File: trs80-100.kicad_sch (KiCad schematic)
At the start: 181 parts, among them CN2 A-7224, CN3 TCS-4480, CN4 TCS-4490, CN6 RS232C, J1 Adapter Jack CN9, M27 4011, M28 4013, M30 TL064, M33 40H157, M34 4584, M35 4584, SW3 SLB-22BP-03, SW4 Reset Switch, SW5 SSP32201, T10 2SC2603, T11 2SC2603, T13 2SC2603, T14 2SC2603(E), T15 2SC2603(E), T16 2SC2603(E), T17 2SC2603(E), T18 2SC2603, T19 2SA1115, T20 2SC2603, T21 2SC2603(E), T22 2SC2603(E), T25 2SC2603, T27 2SC2603, T28 2SA1115, T6 2SC2603, T9 2SC2603

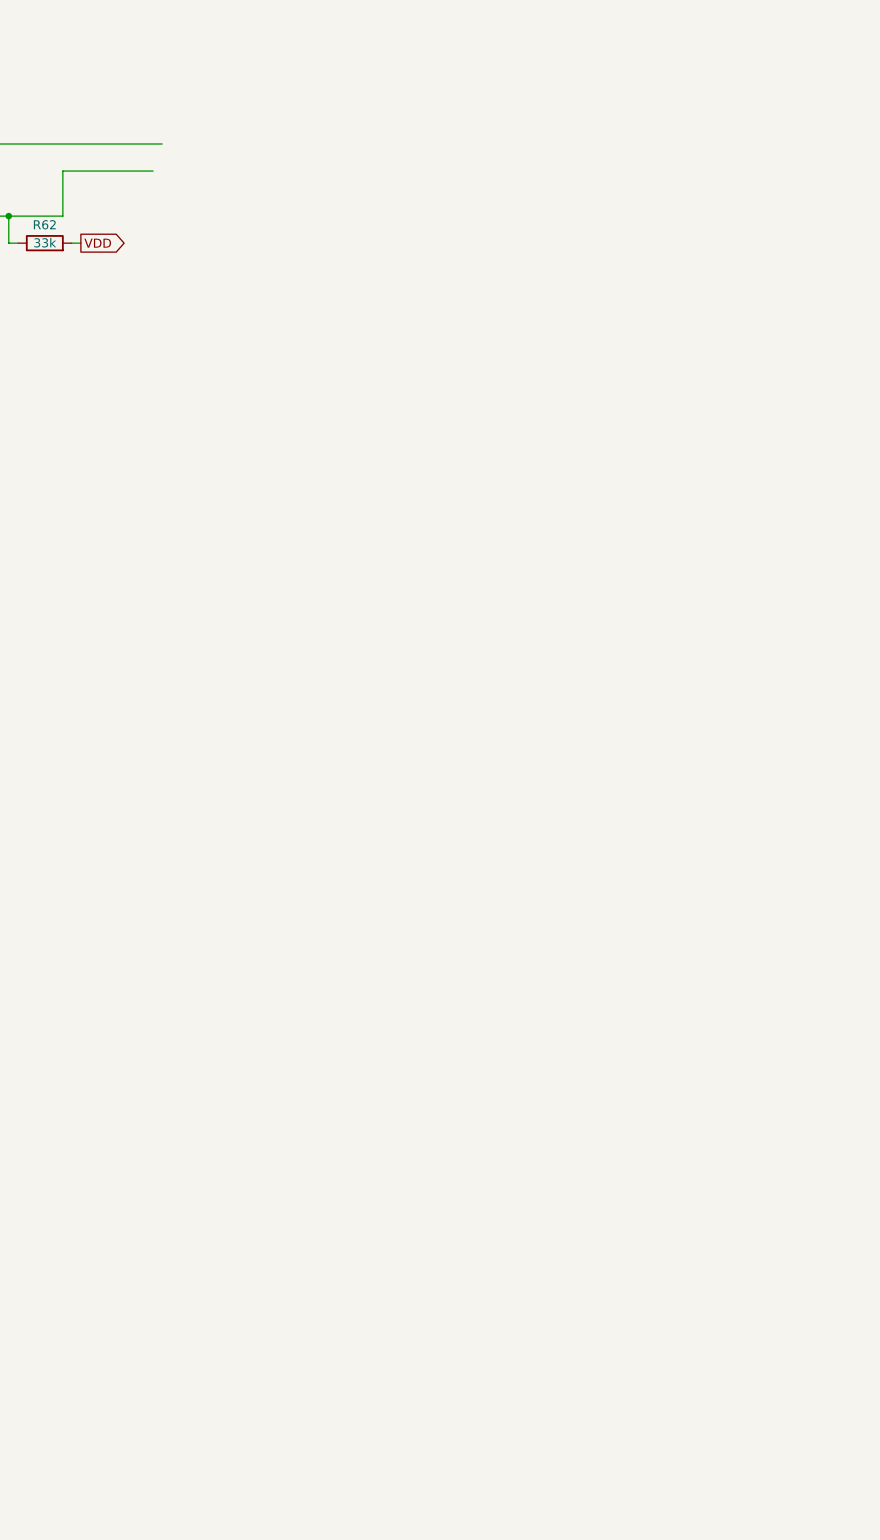
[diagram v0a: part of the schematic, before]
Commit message: Add two different drawings of 40H244 symbol.
Since the schematic is hand-drawn, the pin-out is adapted locally
for the purpose.
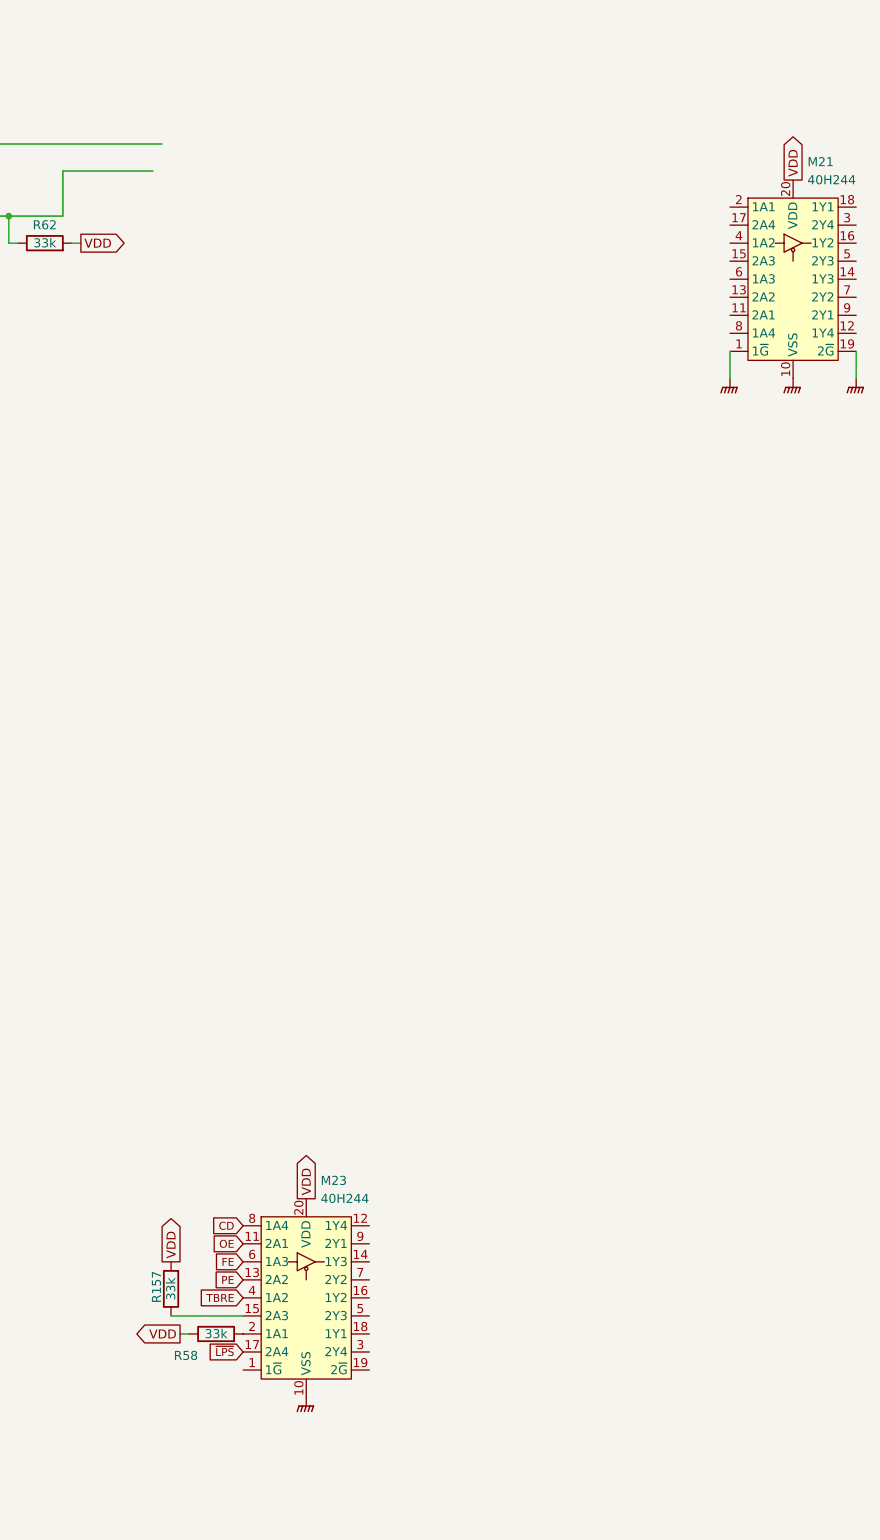
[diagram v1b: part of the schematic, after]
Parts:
- added M21: 40H244, symbol trs80-100:40H244(21)
- added M23: 40H244, symbol trs80-100:40H244(23)
- added R157, R58: 33k, symbol Device:R
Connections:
- net CD: now also M23.8 (1A4)
- net GNDPWR: now also M21.1 (1~{G}), M21.10 (VSS), M21.19 (2~{G}), M23.10 (VSS)
- net VDD: now also M21.20 (VDD), M23.20 (VDD), R157.2, R58.1
- net ~{LPS}: now also M23.17 (2A4)
- new net: M23.2 (1A1), R58.2
- new net: M23.15 (2A3), R157.1
- new net FE: M23.6 (1A3)
- new net OE: M23.11 (2A1)
- new net PE: M23.13 (2A2)
- new net TBRE: M23.4 (1A2)

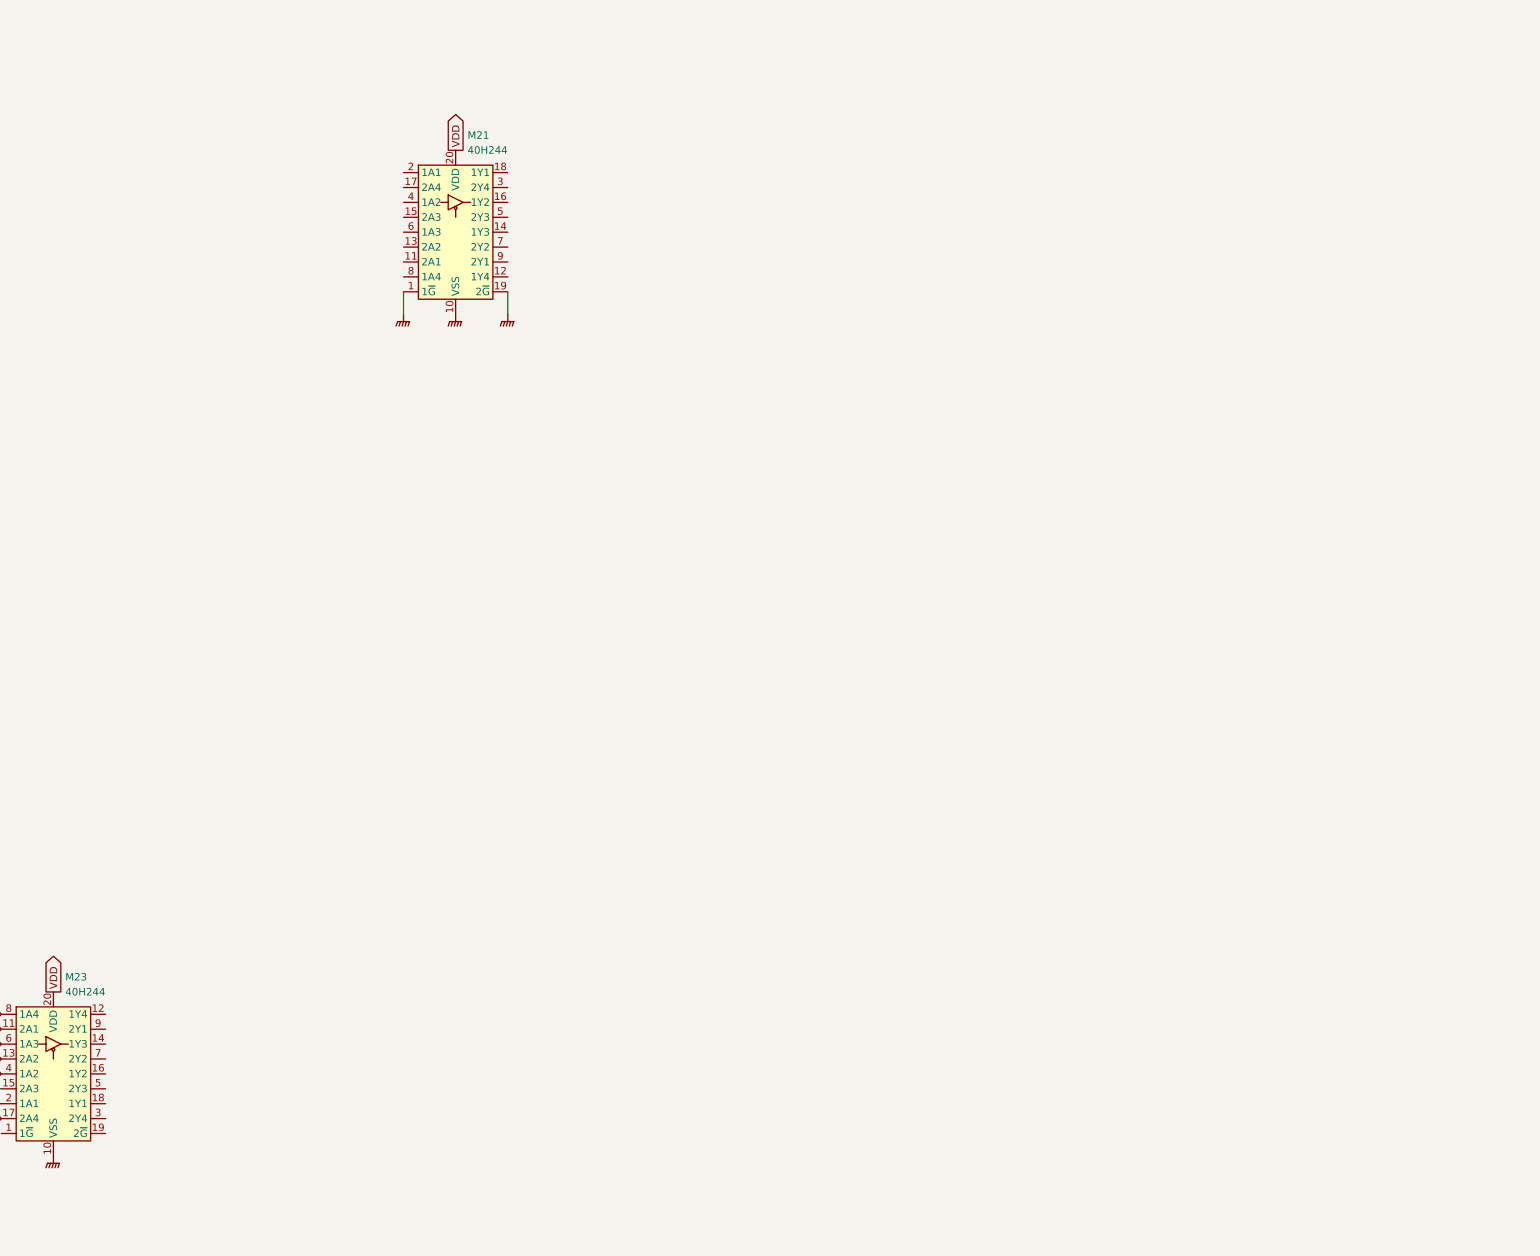
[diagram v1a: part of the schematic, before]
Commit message: Make a keyboard symbol.
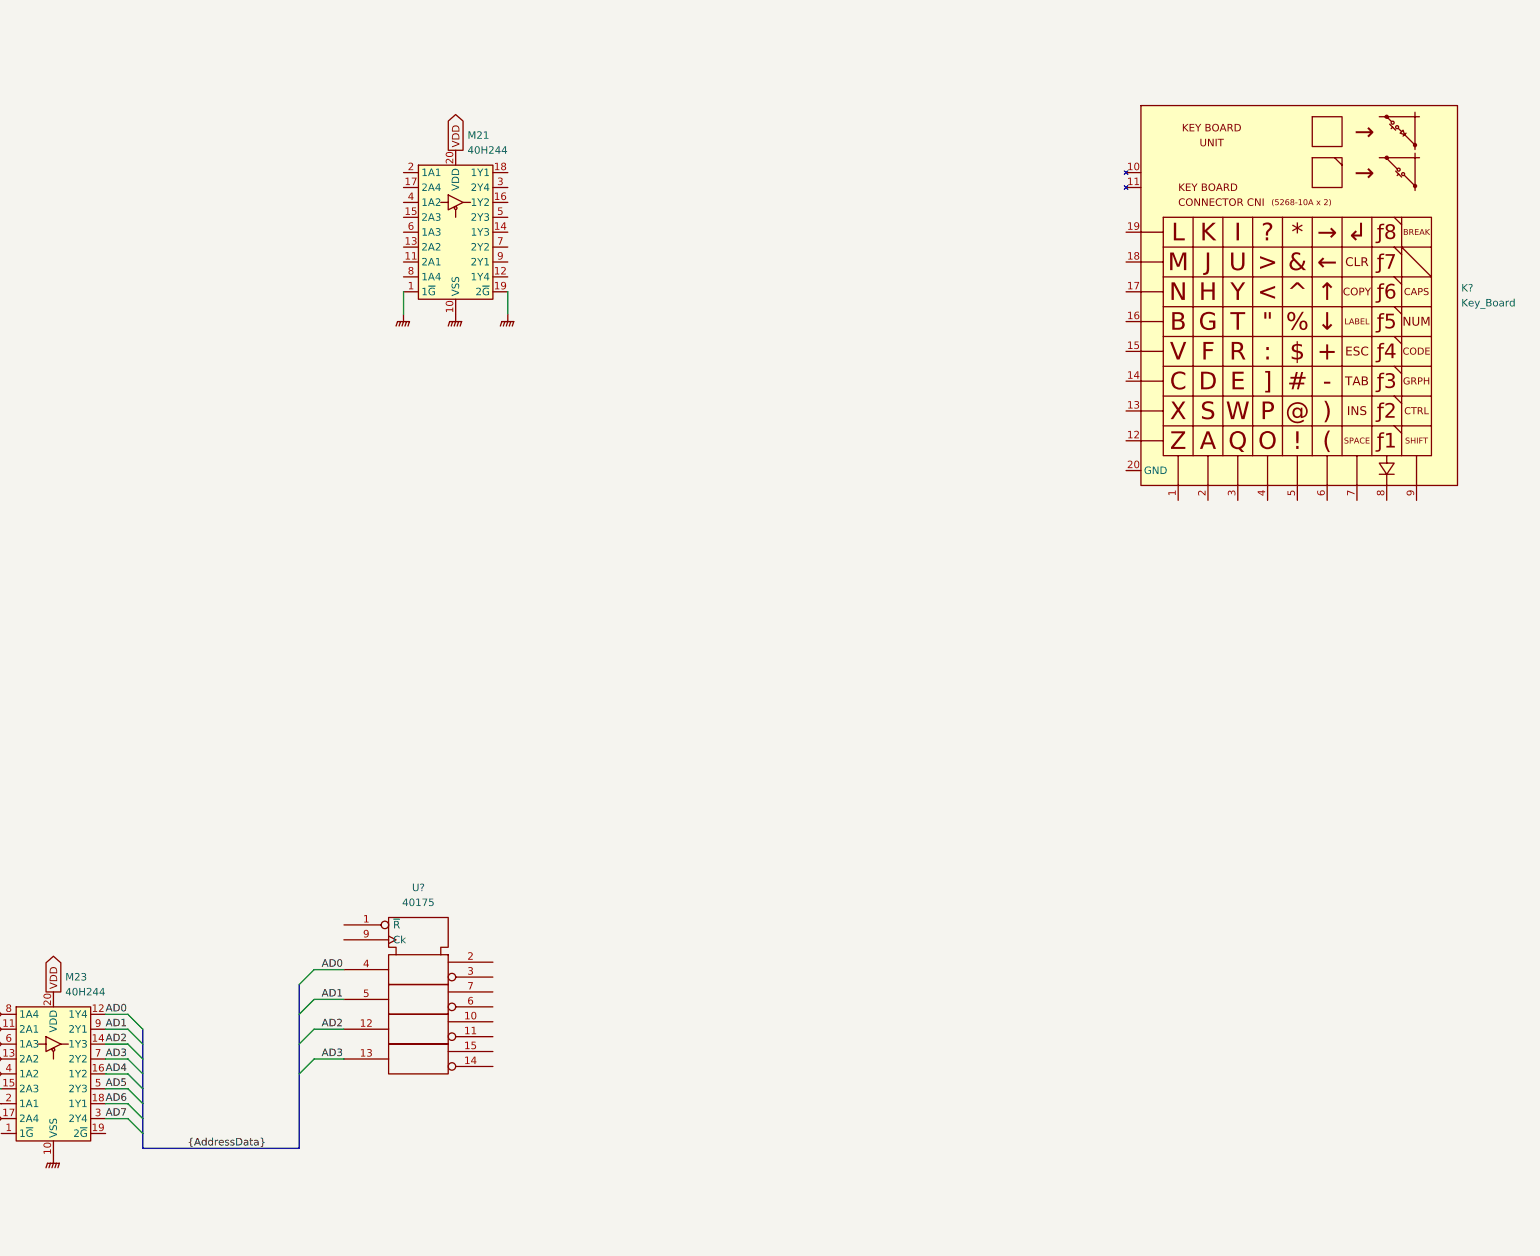
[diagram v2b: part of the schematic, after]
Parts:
- added K?: Key_Board, symbol trs80-100:Key_Board
- added U?: 40175, symbol 4xxx_IEEE:40175
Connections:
- net AD0: now reaches M23.12 (1Y4)
- net AD0: now also U?.4
- net AD2: now reaches M23.14 (1Y3)
- net AD2: now also U?.12
- net AD4: now reaches M23.16 (1Y2)
- net AD6: now reaches M23.18 (1Y1)
- net AD7: now reaches M23.3 (2Y4)
- net AD5: now reaches M23.5 (2Y3)
- net AD3: now reaches M23.7 (2Y2)
- net AD3: now also U?.13
- net AD1: now reaches M23.9 (2Y1)
- net AD1: now also U?.5
- new net Vdd: U?.16 (Vdd)
- new net Vss: U?.8 (Vss)

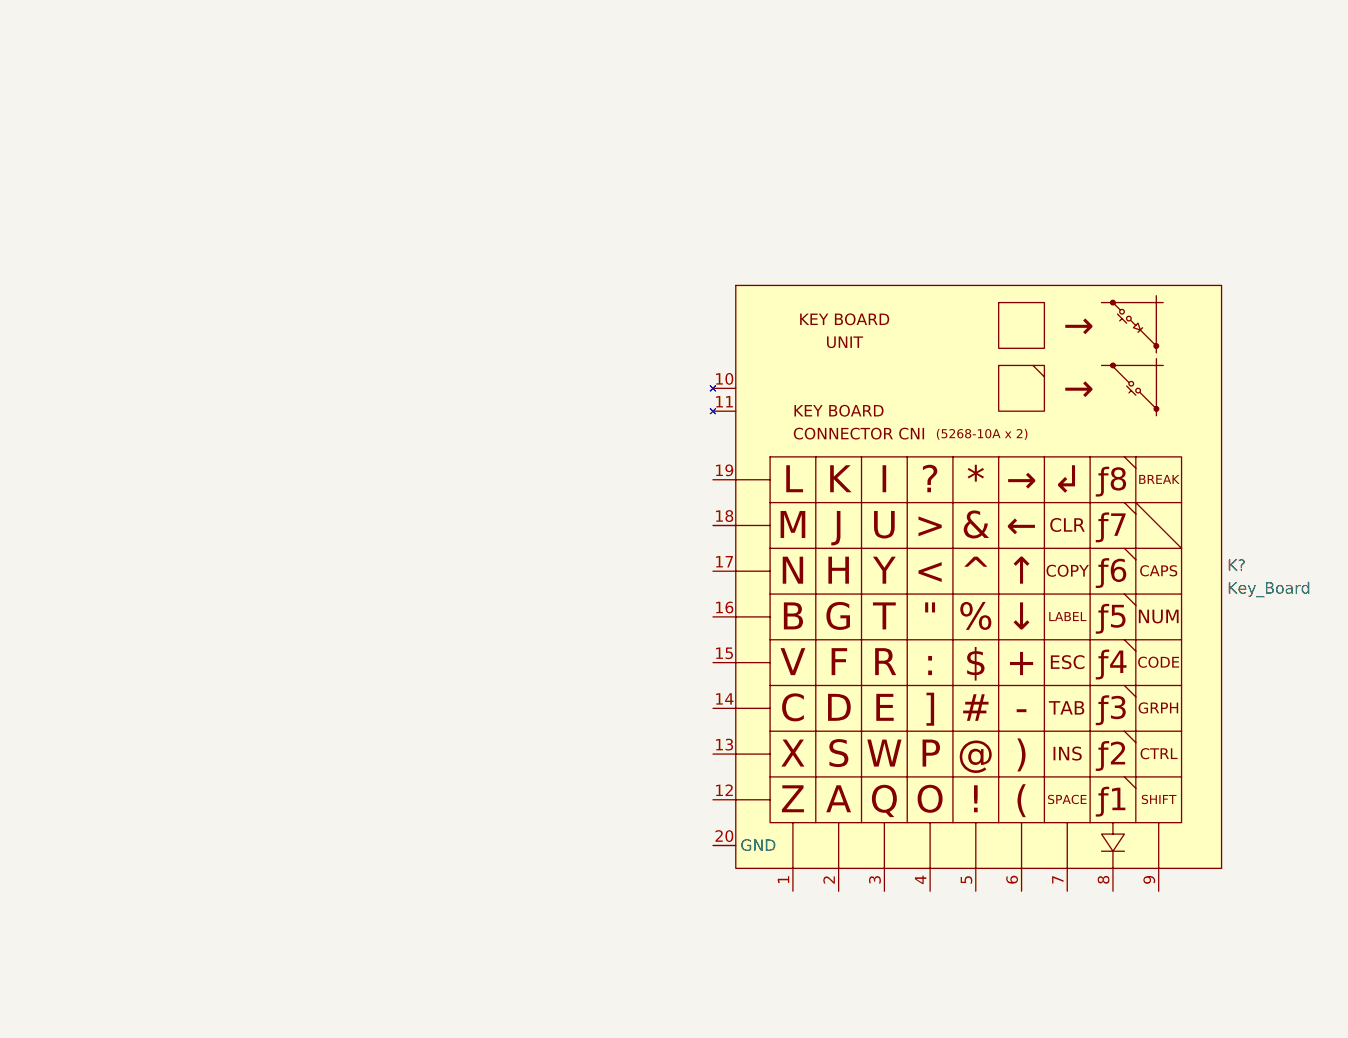
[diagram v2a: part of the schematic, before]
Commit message: Keyboard matrix: wire up RC filters.
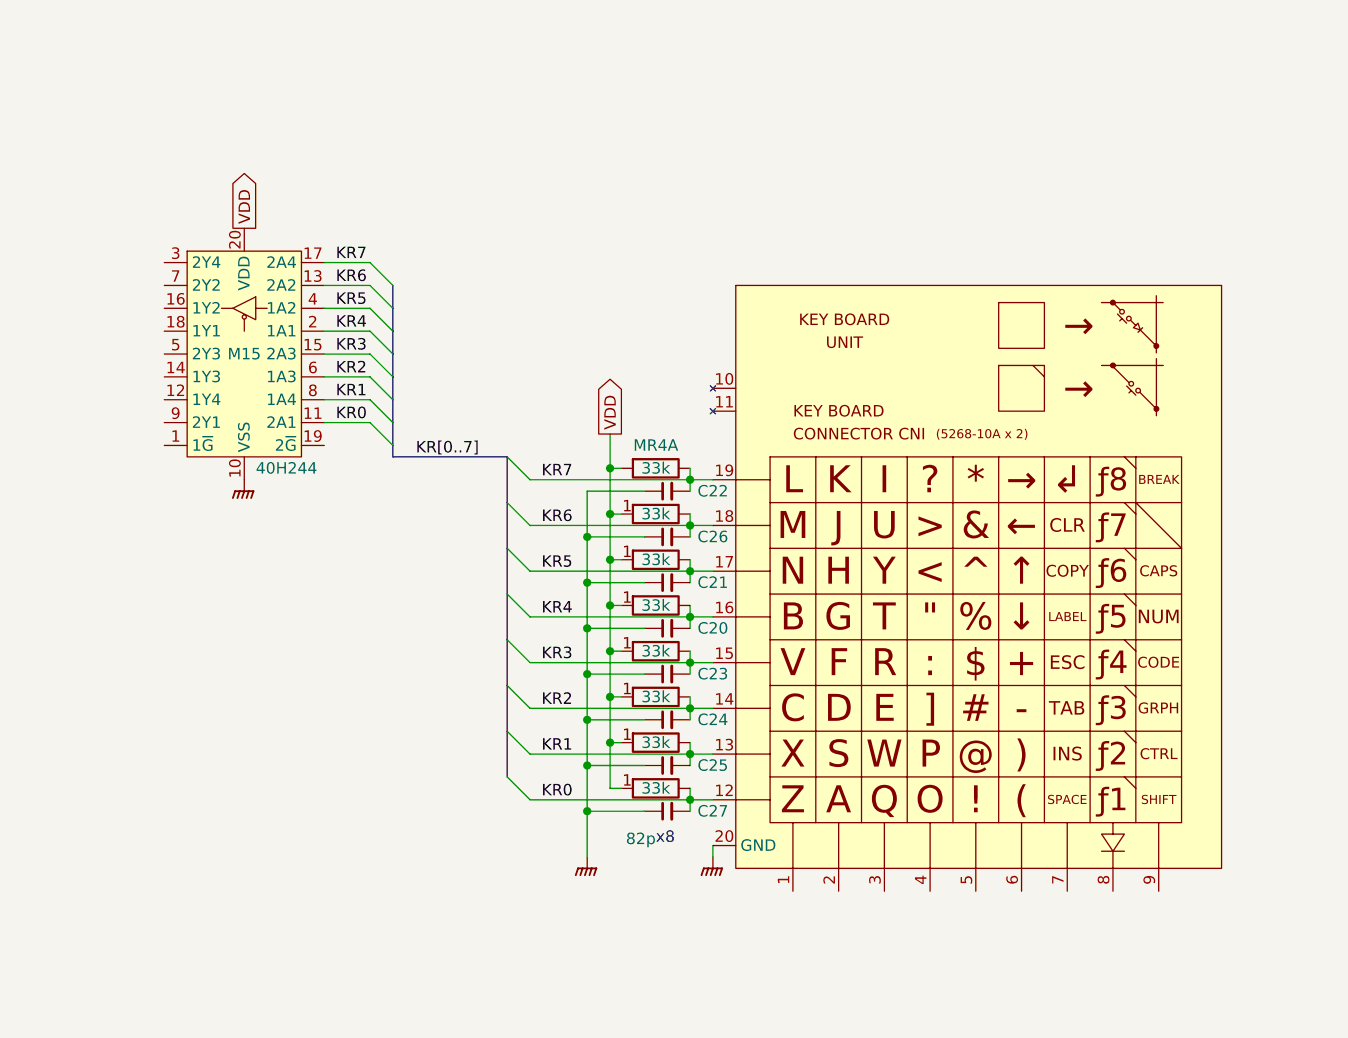
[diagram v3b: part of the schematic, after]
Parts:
- added C20, C21, C22, C23, C24, C25, C26, C27: 82p, symbol trs80-100:C_Tiny
- added M15: 40H244, symbol trs80-100:40H244(15)
- added MR4: 33k, Resistor_THT:R_Array_SIP9, symbol Device:R_Network08_Split
- gave numbers to parts that had none: 1
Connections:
- net GNDPWR: now also K1.20 (GND), C20.1, C21.1, C22.1, C23.1, C24.1, C25.1, C26.1, C27.1, M15.10 (VSS)
- net VDD: now also M15.20 (VDD), MR4.1 (R1.1)
- net KR0: now reaches K1.12
- net KR0: now also C27.2, M15.11 (2A1), MR4.9 (R8.2)
- net KR1: now reaches K1.13
- net KR1: now also C25.2, M15.8 (1A4), MR4.8 (R7.2)
- net KR2: now reaches K1.14
- net KR2: now also C24.2, M15.6 (1A3), MR4.7 (R6.2)
- net KR3: now reaches K1.15
- net KR3: now also C23.2, M15.15 (2A3), MR4.6 (R5.2)
- net KR4: now reaches K1.16
- net KR4: now also C20.2, M15.2 (1A1), MR4.5 (R4.2)
- net KR5: now reaches K1.17
- net KR5: now also C21.2, M15.4 (1A2), MR4.4 (R3.2)
- net KR6: now reaches K1.18
- net KR6: now also C26.2, M15.13 (2A2), MR4.3 (R2.2)
- net KR7: now reaches K1.19
- net KR7: now also C22.2, M15.17 (2A4), MR4.2 (R1.2)
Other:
- note added: "x8"
